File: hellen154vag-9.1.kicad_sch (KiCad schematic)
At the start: 219 parts, among them J1 USB_B_Mini, M1 Module-can-0.1, M2 Module-power5-0.1, M3 Module-mcu-0.1, M4 Module-input-0.1, M5 Module-knock-0.1, M6 Module-output-0.1, M7 Module-ign8-0.1, M8 Module-power12-0.1, P1 368255-2

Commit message: Updated to most recent VAG121 layout, which adds ETB and VR circuits.
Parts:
- removed V51, V52, V70, V71: Pad, hellen-one-common:PAD-TH, symbol hellen-one-common:Pad
- added BT1: BATTERY_CR2032, Battery:BatteryHolder_Keystone_1060_1x2032, symbol art-electro-power:BATTERY_CR2032
- added C1, C15, C16, C2, C6: 100n, hellen-one-common:C0603, symbol hellen-one-common:Cap
- added C10, C11, C12, C13, C14, C7, C8, C9: 10u, Capacitor_SMD:C_0805_2012Metric, symbol hellen-one-common:Cap
- added C17: 10u, hellen-one-common:C0603, symbol hellen-one-common:Cap
- added C3: 220n, hellen-one-common:C0603, symbol hellen-one-common:Cap
- added C4: 10n, hellen-one-common:C0603, symbol hellen-one-common:Cap
- added C5: 5.6n, hellen-one-common:C0603, symbol hellen-one-common:Cap
- added D1, D2, D3, D5, D9: 1N4148WS, hellen-one-common:SOD-323, symbol hellen-one-common:1N4148WS
- added D4, D6, D7, D8: LED-GREEN-0805, hellen-one-common:LED-0805, symbol hellen-one-common:LED
- added G1, G2, G3, G5: PROTO_AREA, hellen-one-common:PROTO_AREA, symbol hellen-one-common:PROTO_AREA
- added G6: LOGO, hellen-one-common:LOGO, symbol hellen-one-common:LOGO
- added J1: USB_B_Mini, hellen-one-common:USB-MINI-B-VERTICAL, symbol hellen-one-common:USB_B_Mini
- added J10: AudioJack_THR, hellen-one-common:Jack_3.5mm_PJ-3250-5A, symbol hellen-one-common:AudioJack_THR
- added J2, J3, J4, J5, J6: Conn_01x01, TestPoint:TestPoint_Pad_D2.0mm, symbol Connector_Generic:Conn_01x01
- added J7, J9: Conn_01x04, Connector_PinHeader_2.54mm:PinHeader_1x04_P2.54mm_Vertical, symbol Connector_Generic:Conn_01x04
- added J8: Conn_01x06, Connector_PinHeader_2.54mm:PinHeader_1x06_P2.54mm_Vertical, symbol Connector_Generic:Conn_01x06
- added M1, M10: Module-can-0.1, hellen-one-can-0.1:can, symbol hellen-one-can-0.1:Module-can-0.1
- added M11: Module-vr-0.1, hellen-one-vr-0.1:vr, symbol hellen-one-vr-0.1:Module-vr-0.1
- added M12: Module-dinput4-0.1, hellen-one-dinput4-0.1:dinput4, symbol hellen-one-dinput4-0.1:Module-dinput4-0.1
- added M2: Module-power5-0.2, hellen-one-power5-0.1:power5, symbol hellen-one-power5-0.1:Module-power5-0.1
- added M3: Module-mcu-0.1, hellen-one-mcu-0.1:mcu, symbol hellen-one-mcu-0.1:Module-mcu-0.1
- added M4: Module-input-0.1, hellen-one-input-0.1:input, symbol hellen-one-input-0.1:Module-input-0.1
- added M5: Module-knock-0.1, hellen-one-knock-0.1:knock, symbol hellen-one-knock-0.1:Module-knock-0.1
- added M6: Module-output-0.1, hellen-one-output-0.1:output, symbol hellen-one-output-0.1:Module-output-0.1
- added unit 3 of M6
- added M7: Module-ign8-0.1, hellen-one-ign8-0.1:ign8, symbol hellen-one-ign8-0.1:Module-ign8-0.1
- added M8: Module-power12-0.1, hellen-one-power12-0.1:power12, symbol hellen-one-power12-0.1:Module-power12-0.1
- added M9: Module-wbo-0.1, hellen-one-wbo-0.1:wbo, symbol hellen-one-wbo-0.1:Module-wbo-0.1
- added R1: 100, hellen-one-common:R0603, symbol hellen-one-common:Res
- added R10, R11, R12, R13: Jumper-Pad-Pad, hellen-one-common:PAD-0805-PAD, symbol hellen-one-common:Jumper-Pad-Pad
- added R14, R15: DNP, hellen-one-common:R1206, symbol hellen-one-common:Res
- added R16, R17: 5.1k, hellen-one-common:R0603, symbol hellen-one-common:Res
- added R18, R19: 4.7k, hellen-one-common:R0603, symbol hellen-one-common:Res
- added R20: 1.6k, hellen-one-common:R0603, symbol hellen-one-common:Res
- added R21: 750, hellen-one-common:R0603, symbol hellen-one-common:Res
- added R5: 100k, hellen-one-common:R0603, symbol hellen-one-common:Res
- added R6, R7: 2.7k, hellen-one-common:R0603, symbol hellen-one-common:Res
- added S1, S2: Button_SPST, hellen-one-common:SMD-2_2.9x3.9x1.7, symbol hellen-one-common:Button_SPST
- added U1: L6205PD, hellen-one-common:SO20POWER, symbol hellen-one-common:L6205PD
- added U2: LPS25HB, Package_LGA:ST_HLGA-10_2.5x2.5mm_P0.6mm_LayoutBorder3x2y, symbol Sensor_Pressure:LPS25HB
- added U3: MCP6002-xSN, Package_SO:SOIC-8_3.9x4.9mm_P1.27mm, symbol Amplifier_Operational:MCP6002-xSN
- added VIN1, VIN2, VIN3, VIN4, VOUT1, VOUT2, VOUT3: Pad, hellen-one-common:PAD-TH, symbol hellen-one-common:Pad
- P1: footprint rusEFI_Lib:284617-1 -> hellen121vag:368255-2
- R2, R3, R4, R8, R9: LCSC C17477 -> C17477
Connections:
- net +12V: now also D5.1 (K), D8.1 (A), G3.1, G3.11, G3.6, J2.1 (Pin_1), M2.V1 (V12), M8.V1 (V12)
- net +3V3: now also C15.2, D7.1 (A), G3.13, G3.3, G3.8, J4.1 (Pin_1), M3.N16 (V33), R18.1, R19.1, S1.2, U2.1 (VDDio), U2.10 (VDD), U2.6 (~CS)
- net +5V: now also C16.2, D6.1 (A), G3.12, G3.2, G3.7, J3.1 (Pin_1), M1.V1 (V5), M10.V1 (V5), M11.N1 (V5), M12.V1 (V5), M2.V2 (V5), M3.S1 (V5), M4.E2 (V5), M6.W14 (V5), M8.E1 (V5), M9.W1 (V5_IN), U3.8 (V+)
- net A1: now also M3.S30 (IN_O2S2), M4.N4 (O2S2)
- net A2: now also M3.S22 (IN_MAP3), M4.N12 (MAP3)
- net A3: now also M3.S26 (IN_AUX3), M4.N8 (AUX3)
- net A4: now also M3.S23 (IN_RES3), M4.N11 (RES3)
- net AFR: now also M3.S16 (IN_O2S), M4.N18 (O2S)
- net BOOT0: now also M3.N28 (BOOT0), S1.1
- net CAM1: now also M3.S15 (IN_CAM), M4.N19 (CAM)
- net CAM2: now also M3.S27 (IN_AUX4), M4.N7 (AUX4)
- net CAN_RX: now also M1.V6 (CAN_RX), M3.N2 (CAN_RX)
- net CAN_TX: now also M1.V5 (CAN_TX), M3.N3 (CAN_TX)
- net CAN_VIO: now also M1.V2 (CAN_VIO), M3.N1 (CAN_VIO)
- net CE: now also M3.E22 (OUT_IO8), M6.W25 (LOW6_DIODE)
- net CLT: now also M3.S18 (IN_CLT), M4.N16 (CLT)
- net CRANK: now also M3.S13 (IN_CRANK), M4.N21 (CRANK)
- net D1: now also M12.W4 (OUT_D1), M3.S3 (IN_D1)
- net D2: now also M12.W3 (OUT_D2), M3.S4 (IN_D2)
- net D3: now also M12.W2 (OUT_D3), M3.S5 (IN_D3)
- net D4: now also M12.W1 (OUT_D4), M3.S6 (IN_D4)
- net FUEL_CONSUM: now also M3.E19 (OUT_PWM7), M6.W22 (PP2)
- net GND: now also BT1.2 (-), C1.1, C10.1, C11.1, C12.1, C13.1, C14.1, C15.1, C16.1, C2.1, C5.1, C6.1, C7.1, C8.1, C9.1, G3.10, G3.14, G3.15, G3.4, G3.5, G3.9, J1.5 (GND), J10.S, J5.1 (Pin_1), J6.1 (Pin_1), J8.3 (Pin_3), M1.E1 (GND), M10.E1 (GND), M11.G (GND), M12.G (GND), M12.J1 (PULL_D1), M12.J2 (PULL_D2), M12.J3 (PULL_D3), M12.J4 (PULL_D4), M2.G (GND), M3.S2 (GND), M4.E1 (GND), M5.E2 (GND), M6.G (GND), M6.S3 (GND), M7.G (GND), M8.S1 (GND), M9.E6 (LSU_H-), M9.G (GND), R16.2, R17.2, R20.2, R21.2, S2.2, U1.1 (GND@1), U1.10 (GND@2), U1.11 (GND@3), U1.13 (SENSEB), U1.20 (GND@4), U1.8 (SENSEA), U1.SLUG1 (SLUG@1), U1.SLUG2 (SLUG@2), U1.SLUG3 (SLUG@3), U2.3 (GND), U2.5 (SA0/MISO), U2.8 (GND), U2.9 (GND), U3.4 (V-), U3.5 (+)
- net GNDA: now also M3.S32 (GNDA), M4.J11 (PULL_RES3), M4.J12 (PULL_MAP3), M4.J13 (PULL_MAP2), M4.J14 (PULL_MAP1), M4.J2 (PULL_GNDA), M4.J22 (PULL_KNOCK), M4.J24 (PULL_SENS3), M4.J3 (PULL_RES2), M4.J4 (PULL_O2S2), M4.J6 (PULL_RES1), M4.J8 (PULL_AUX3), M4.N2 (GNDA), R6.2, R7.2
- net IAT: now also M3.S19 (IN_IAT), M4.N15 (IAT)
- net IDLE: now also M3.E18 (OUT_PWM6), M6.W38 (LOW3_DUAL)
- net IGN1: now also M3.W1 (OUT_IGN1), M7.V8 (IGN1)
- net IGN2: now also M3.W2 (OUT_IGN2), M7.V7 (IGN2)
- net IGN3: now also M3.W3 (OUT_IGN3), M7.V6 (IGN3)
- net IGN4: now also M3.W4 (OUT_IGN4), M7.V5 (IGN4)
- net IGN5: now also M3.W5 (OUT_IGN5), M7.V4 (IGN5)
- net IGN6: now also M3.W6 (OUT_IGN6), M7.V3 (IGN6)
- net IGN7: now also M3.W7 (OUT_IGN7), M7.V2 (IGN7)
- net IGN8: now also M3.W8 (OUT_IGN8), M7.V1 (IGN8)
- net IGN_V33: now also M3.W10 (IGN_V33), M7.V10 (V33)
- net IGN_V5: now also M3.W9 (IGN_V5), M7.V9 (VCC)
- net INJ1: now also M3.E25 (OUT_INJ1)
- net INJ2: now also M3.E26 (OUT_INJ2)
- net INJ3: now also M3.E29 (OUT_INJ3)
- net INJ4: now also M3.E30 (OUT_INJ4)
- net INJ5: now also M3.E31 (OUT_INJ5)
- net INJ6: now also M3.E32 (OUT_INJ6)
- net INJ7: now also M3.E33 (OUT_INJ7)
- net INJ8: now also M3.E34 (OUT_INJ8)
- net IN_A1: now also M4.S25 (IN_O2S2), VIN1.1 (Pin_1)
- net IN_A2: now also M4.S19 (IN_MAP3), VIN2.1 (Pin_1)
- net IN_A3: now also M4.S20 (IN_AUX3), VIN3.1 (Pin_1)
- net IN_A4: now also M4.S22 (IN_RES3), VIN4.1 (Pin_1)
- net IN_AFR: now also M4.S9 (IN_O2S)
- net IN_CAM1: now also P1.86, M4.S5 (IN_CAM)
- net IN_CAM2: now also M4.S21 (IN_AUX4)
- net IN_CLT: now also P1.93, M4.S15 (IN_CLT), R6.1
- net IN_CRANK: now also M11.W2 (OUT_VR1), M4.S8 (IN_CRANK), R14.2; no longer P1.82
- net IN_D1: now also M12.V2 (IN_D1)
- net IN_D2: now also M12.V3 (IN_D2)
- net IN_D3: now also M12.V4 (IN_D3)
- net IN_D4: now also M12.V5 (IN_D4)
- net IN_IAT: now also P1.26, M4.S16 (IN_IAT), R7.1
- net IN_KNOCK1: now also M4.S7 (IN_KNOCK), M5.E3 (OUT_KNOCK), U3.3 (+)
- net IN_KNOCK1_RAW: now also M5.W1 (IN_KNOCK)
- net IN_KNOCK2: now also M4.S3 (IN_SENS3)
- net IN_MAF: now also P1.29, M4.S11 (IN_MAP1)
- net IN_MAP2: now also P1.101, M4.S12 (IN_MAP2)
- net IN_PPS1: now also M4.S24 (IN_PPS)
- net IN_PPS2: now also M4.S18 (IN_AUX2)
- net IN_RES1: now also M4.S23 (IN_RES1)
- net IN_RES2: now also M4.S26 (IN_RES2)
- net IN_TPS1: now also P1.92, M4.S10 (IN_TPS)
- net IN_TPS2: now also P1.84, M4.S17 (IN_AUX1)
- net IN_VIGN: now also D3.1 (K), D4.1 (A), M8.V3 (IN_VIGN)
- net IN_VSS: now also M4.S6 (IN_VSS)
- net KNOCK1: now also M3.S12 (IN_KNOCK), M4.N22 (KNOCK)
- net KNOCK2: now also M4.N24 (SENS3)
- net MAF: now also M3.S20 (IN_MAP1), M4.N14 (MAP1)
- net MAIN: now also M3.E6 (OUT_IO3), M6.W40 (LOW5_MAIN)
- net MAP2: now also M3.S21 (IN_MAP2), M4.N13 (MAP2)
- net NRESET: now also C6.2, M3.N24 (nReset), S2.1
- net OUT1: now also M3.E7 (OUT_IO5), M6.W39 (LOW7_HIGH1)
- net OUT2: now also M3.E9 (OUT_IO6), M6.W37 (LOW8_HIGH2)
- net OUT3: now also M3.E28 (OUT_PWM8), M6.W21 (LOW1)
- net OUT_COIL_A1: no longer P1.117
- net OUT_COIL_A2: no longer P1.118
- net OUT_FUEL_CONSUM: now also M6.S6 (OUT_PP2)
- net OUT_IGN1: now also P1.102, M7.S8 (OUT_IGN1)
- net OUT_IGN2: now also P1.7, M7.S7 (OUT_IGN2)
- net OUT_IGN3: now also P1.111, M7.S6 (OUT_IGN3)
- net OUT_IGN4: now also P1.94, M7.S5 (OUT_IGN4)
- net OUT_IGN5: now also M7.S4 (OUT_IGN5)
- net OUT_IGN6: now also M7.S3 (OUT_IGN6)
- net OUT_IGN7: now also M7.S2 (OUT_IGN7)
- net OUT_IGN8: now also M7.S1 (OUT_IGN8)
- net OUT_PUMP: now also M6.S10 (OUT_LOW11)
- net OUT_TACH: now also M6.W6 (OUT_PP1)
- net OUT_VVT1_1: now also M6.S13 (OUT_LOW12), M6.S14 (OUT_LOW9)
- net OUT_VVT1_2: now also M6.W1 (OUT_LOW2), M6.W2 (OUT_LOW10)
- net OUT_VVT2_B1: now also M6.S5 (OUT_SOLENOID_B2)
- net OUT_VVT2_B2: now also M6.S4 (OUT_SOLENOID_B1)
- net OUT_WASTEGATE: now also P1.104
- net PPS1: now also M3.S29 (IN_PPS), M4.N5 (PPS)
- net PPS2: now also M3.S25 (IN_AUX2), M4.N9 (AUX2)
- net PUMP: now also M3.E8 (OUT_IO1), M6.W35 (LOW11)
- net RES1: now also M3.S28 (IN_RES1), M4.N6 (RES1)
- net RES2: now also M3.S31 (IN_RES2), M4.N3 (RES2)
- net TACH: now also M3.E27 (OUT_PWM1), M6.W28 (PP1)
- net TPS1: now also M3.S17 (IN_TPS), M4.N17 (TPS)
- net TPS2: now also M3.S24 (IN_AUX1), M4.N10 (AUX1)
- net USBM: now also J1.2 (D-), M3.N31 (USB1M)
- net USBP: now also J1.3 (D+), M3.N30 (USB1P)
- net V12_PERM: now also M8.V4 (V12_PERM)
- net V12_RAW: no longer F1.2, F2.2
- net V5A: no longer P1.53, P1.73, P1.83, P1.98
- net VBAT: now also D9.1 (K), M3.N17 (VBAT), M8.V2 (VBAT)
- net VBUS: now also J1.1 (VBUS), M3.N29 (VBUS)
- net VIGN: now also M3.S7 (VIGN), M8.V5 (VIGN)
- net VREF1: now also M4.S14 (VREF1), R15.2
- net VREF2: now also M4.S13 (VREF2), M5.W2 (VREF)
- net VSS: now also M3.S14 (IN_VSS), M4.N20 (VSS)
- net VVT1_1: now also M3.E10 (OUT_IO10), M6.W27 (LOW9), M6.W36 (LOW12)
- net VVT1_2: now also M3.E21 (OUT_IO7), M6.W26 (LOW10), M6.W29 (LOW2)
- net VVT2_B1: now also M3.E17 (OUT_PWM5), M6.W30 (SOLENOID_B2)
- net VVT2_B2: now also M3.E16 (OUT_PWM4), M6.W31 (SOLENOID_B1)
- net WASTEGATE: now also M3.E12 (OUT_IO2), M6.W34 (LOW4_DUAL)
- net at P1.21: now also R2.1, R8.1
- net at P1.23: now also R3.1
- net at P1.51: now also R10.1
- net at P1.52: now also R11.1
- net CAN-: now reaches P1.58
- net CAN-: now also M1.S1 (CANL), M10.S1 (CANL)
- net CAN+: now reaches P1.60
- net CAN+: now also M1.S2 (CANH), M10.S2 (CANH)
- net at P1.70: now also R12.1
- net at P1.71: now also R13.1
- net +5VA: now reaches P1.72
- net +5VA: now also P1.53, P1.73, P1.83, P1.98, M3.S33 (V5A), M4.E5 (V5A), M4.J1 (PULL_V5A), M4.J10 (PULL_AUX1), M4.J17 (PULL_CAM), M4.J18 (PULL_VSS), M4.J19 (PULL_TPS), M4.J20 (PULL_O2S), M4.J21 (PULL_CRANK), M4.J5 (PULL_PPS), M4.J7 (PULL_AUX4), M4.J9 (PULL_AUX2), M4.N1 (V5A), M5.E1 (V5A)
- net IN_CRANK-: now reaches P1.90
- net IN_CRANK-: now also M11.E1 (IN_VR1-), R15.1
- net LSU_HEAT-: now reaches P1.5
- net LSU_HEAT-: now also M9.E5 (LSU_H+)
- new net: BT1.1 (+), D9.2 (A)
- new net: D5.2 (A), D8.2 (K), R17.1
- new net: D6.2 (K), R20.1
- new net: G5.1, G5.11, G5.6
- new net: G5.10, G5.15, G5.5
- new net: G5.12, G5.2, G5.7
- new net: G5.13, G5.3, G5.8
- new net: G5.14, G5.4, G5.9
- new net: D3.2 (A), D4.2 (K), R16.1
- new net: G1.1, G1.11, G1.6
- new net: G1.10, G1.15, G1.5
- new net: G1.12, G1.2, G1.7
- new net: G1.13, G1.3, G1.8
- new net: G1.14, G1.4, G1.9
- new net: M3.N18 (I2C_SDA), R19.2, U2.4 (SDA/MOSI)
- new net: M3.N19 (I2C_SCL), R18.2, U2.2 (SCL/SCLK)
- new net: U3.6 (-), U3.7
- new net: C5.2, R5.2, U1.16 (ENB), U1.5 (ENA)
- new net: M6.S8 (OUT_LOW1), VOUT3.1 (Pin_1)
- new net: M6.S12 (OUT_LOW8_PULLUP), VOUT2.1 (Pin_1)
- new net: D1.1 (K), D2.2 (A), R1.1
- new net: C4.1, U1.4 (VCP)
- new net: C4.2, R1.2
- new net: M6.W9 (OUT_LOW7_PULLUP), VOUT1.1 (Pin_1)
- new net: C17.2, U3.1, U3.2 (-)
- new net: C17.1, J10.T
- new net: C3.1, D2.1 (K), U1.17 (VBOOT)
- new net: G2.1, G2.11, G2.6
- new net: G2.10, G2.15, G2.5
- new net: G2.12, G2.2, G2.7
- new net: G2.13, G2.3, G2.8
- new net: G2.14, G2.4, G2.9
- new net: D7.2 (K), R21.1
- new net: M10.V2 (CAN_VIO), M9.W2 (CAN_VIO)
- new net: M10.V6 (CAN_RX), M9.W3 (CAN_RX)
- new net: M10.V5 (CAN_TX), M9.W4 (CAN_TX)
- new net: J8.5 (Pin_5), M9.W5 (nReset)
- new net: J8.4 (Pin_4), M9.W6 (SWDIO)
- new net: J8.2 (Pin_2), M9.W7 (SWCLK)
- new net: J8.1 (Pin_1), M9.W8 (V33_OUT)
- new net +12V_PROT: M6.W5 (V12P)
- new net +12V_RAW: C1.2, C10.2, C11.2, C12.2, C13.2, C14.2, C2.2, C3.2, C7.2, C8.2, C9.2, D1.2 (A), F1.2, F2.2, M6.S11 (V12_RAW), M8.E2 (V12_RAW), U1.19 (VSB), U1.2 (VSA)
- new net +ETB: M3.E14 (OUT_PWM2), U1.15 (IN2B), U1.7 (IN2A)
- new net +ETB_OUT: P1.117, U1.18 (OUT2B), U1.3 (OUT2A)
- new net -ETB: M3.E15 (OUT_PWM3), U1.14 (IN1B), U1.6 (IN1A)
- new net -ETB_OUT: P1.118, U1.12 (OUT1B), U1.9 (OUT1A)
- new net ETB_EN: M3.E13 (OUT_IO12), R5.1
- new net IN_CRANK+: M11.E2 (IN_VR1+), P1.82, R14.1
- new net IO1: J9.4 (Pin_4), M3.N12 (IO1)
- new net IO2: J9.3 (Pin_3), M3.N13 (IO2)
- new net IO3: J9.2 (Pin_2), M3.N14 (IO3)
- new net IO4: J9.1 (Pin_1), M3.N15 (IO4)
- new net LSU_CALIBR_RES: M9.E4 (LSU_Rtrim), R13.2
- new net LSU_PUMP_I: M9.E3 (LSU_Ip), R11.2
- new net LSU_SENSOR_U: M9.E1 (LSU_Un), R12.2
- new net LSU_SENSOR_U/PUMP_I: M9.E2 (LSU_Vm), R10.2
- new net SPI2_CS: J7.1 (Pin_1), M3.N23 (SPI2_CS)
- new net SPI2_MISO: J7.3 (Pin_3), M3.N21 (SPI2_MISO)
- new net SPI2_MOSI: J7.2 (Pin_2), M3.N22 (SPI2_MOSI)
- new net SPI2_SCK: J7.4 (Pin_4), M3.N20 (SPI2_SCK)
- no-connect marks 72 -> 126
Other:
- note added: "Analog inputs (sensors)"
- note added: "Board info"
- note added: "Bus types"
- note added: "Discrete inputs"
- note added: "ETB driver"
- note added: "General purpose bus"
- note added: "Ignition"
- note added: "Injection"
- note added: "LEDs"
- note added: "Ouputs"
- note added: "Power"
- note added: "Prototype areas"
- note added: "http://rusefi.com/s/hellen121vag"
- note added: "to ETB driver"
- moved on the sheet: C1, D1, J1, M1, M2, M3A, M3B, M3C, M3D, M4A, M4B, M4C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

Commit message: MISC net names were connected, like ETB and VR nets are now connected.
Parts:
- removed C1: Cap, hellen-one-common:C0603, symbol hellen-one-common:Cap
- removed D1: D_TVS_Array_4, hellen-one-common:SOT23-6, symbol hellen-one-common:D_TVS_Array_4
- removed J1: USB_B_Mini, hellen-one-common:USB-MINI-B-VERTICAL, symbol hellen-one-common:USB_B_Mini
- removed M1: Module-can-0.1, hellen-one-can-0.1:can, symbol hellen-one-can-0.1:Module-can-0.1
- removed M2: Module-power5-0.1, hellen-one-power5-0.1:power5, symbol hellen-one-power5-0.1:Module-power5-0.1
- removed M3: Module-mcu-0.1, hellen-one-mcu-0.1:mcu, symbol hellen-one-mcu-0.1:Module-mcu-0.1
- removed M4: Module-input-0.1, hellen-one-input-0.1:input, symbol hellen-one-input-0.1:Module-input-0.1
- removed M5: Module-knock-0.1, hellen-one-knock-0.1:knock, symbol hellen-one-knock-0.1:Module-knock-0.1
- removed M6: Module-output-0.1, hellen-one-output-0.1:output, symbol hellen-one-output-0.1:Module-output-0.1
- removed M7: Module-ign8-0.1, hellen-one-ign8-0.1:ign8, symbol hellen-one-ign8-0.1:Module-ign8-0.1
- removed M8: Module-power12-0.1, hellen-one-power12-0.1:power12, symbol hellen-one-power12-0.1:Module-power12-0.1
- removed R1, R5: Res_Array_4, hellen-one-common:R0603-4, symbol hellen-one-common:Res_Array_4
- removed R6, R7: Res, hellen-one-common:R0603, symbol hellen-one-common:Res
- removed S1, S2: Button_SPST, hellen-one-common:SMD-2_2.9x3.9x1.7, symbol hellen-one-common:Button_SPST
- removed VIN1, VIN2, VIN3, VIN4, VOUT1, VOUT2, VOUT3: Pad, hellen-one-common:PAD-TH, symbol hellen-one-common:Pad
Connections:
- net +ETB_OUT: now also W?.2
- net -ETB_OUT: now also W?.2
- net CAN+: no longer M1.S2 (CANH)
- net CAN-: no longer M1.S1 (CANL)
- net CANH: now also M1.S2 (CANH)
- net CANL: now also M1.S1 (CANL)
- net INJ6: now also M6.W17 (INJ6)
- net INJ7: now also M6.W16 (INJ7)
- net INJ8: now also M6.W15 (INJ8)
- net OUT_CE: now also M6.W3 (OUT_LOW6_DIODE)
- net OUT_IDLE: now also M6.S7 (OUT_LOW3_DUAL)
- net OUT_INJ6: now also M6.S15 (OUT_INJ6)
- net OUT_INJ7: now also M6.W12 (OUT_INJ7), W?.2
- net OUT_INJ8: now also M6.W11 (OUT_INJ8), W?.2
- net OUT_MAIN: now also M6.W13 (OUT_LOW5_MAIN)
- net OUT_WASTEGATE: now also M6.W4 (OUT_LOW4_DUAL)
- no-connect marks 126 -> 72

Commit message: This time I really did connect the VR net.
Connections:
- net IN_CRANK+: now also W?.2
- net IN_CRANK-: now also W?.2
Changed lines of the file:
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@@
     (stroke (width 0) (type solid) (color 0 0 0 0))
   )
+  (wire (pts (xy 45.72 278.13) (xy 56.515 278.13))
+    (stroke (width 0) (type solid) (color 0 0 0 0))
+  )
   (wire (pts (xy 45.72 344.17) (xy 51.435 344.17))
     (stroke (width 0) (type solid) (color 0 0 0 0))
@@
     (effects (font (size 1.27 1.27)) (justify left bottom))
   )
+  (label "IN_CRANK+" (at 45.72 280.67 0)
+    (effects (font (size 1.27 1.27)) (justify left bottom))
+  )
   (label "INJ_B2_HIGH" (at 45.72 289.56 0)
     (effects (font (size 1.27 1.27)) (justify left bottom))
@@
     (effects (font (size 1.27 1.27)) (justify left bottom))
   )
+  (label "IN_CRANK-" (at 45.72 322.58 0)
+    (effects (font (size 1.27 1.27)) (justify left bottom))
+  )
   (label "INJ_B1_HIGH" (at 45.72 331.47 0)
     (effects (font (size 1.27 1.27)) (justify left bottom))
@@
       (effects (font (size 1.27 1.27)) hide)
     )
-    (property "Value" "V5A" (id 1) (at 50.0444 320.4083 0))
+    (property "Value" "V5A" (id 1) (at 50.0444 319.7733 90))
     (property "Footprint" "" (id 2) (at 45.72 320.04 0)
       (effects (font (size 1.27 1.27)) hide)
@@
     (pin "1")
   )
-  (symbol (lib_id "power:GND") (at 45.72 278.13 90) (unit 1)
-    (in_bom yes) (on_board yes)
-    (property "Reference" "#PWR?" (id 0) (at 52.07 278.13 0)
-      (effects (font (size 1.27 1.27)) hide)
-    )
-    (property "Value" "GND" (id 1) (at 49.6634 278.0792 0))
-    (property "Footprint" "" (id 2) (at 45.72 278.13 0)
-      (effects (font (size 1.27 1.27)) hide)
-    )
-    (property "Datasheet" "" (id 3) (at 45.72 278.13 0)
-      (effects (font (size 1.27 1.27)) hide)
-    )
-    (pin "1")
-  )
   (symbol (lib_id "power:GND") (at 50.8 386.08 90) (unit 1)
     (in_bom yes) (on_board yes)
@@
     (pin "1")
   )
+  (symbol (lib_id "power:GND") (at 56.515 278.13 90) (unit 1)
+    (in_bom yes) (on_board yes)
+    (property "Reference" "#PWR?" (id 0) (at 62.865 278.13 0)
+      (effects (font (size 1.27 1.27)) hide)
+    )
+    (property "Value" "GND" (id 1) (at 60.4584 278.0792 0))
+    (property "Footprint" "" (id 2) (at 56.515 278.13 0)
+      (effects (font (size 1.27 1.27)) hide)
+    )
+    (property "Datasheet" "" (id 3) (at 56.515 278.13 0)
+      (effects (font (size 1.27 1.27)) hide)
+    )
+    (pin "1")
+  )
   (symbol (lib_id "power:GNDA") (at -417.195 80.645 90) (mirror x) (unit 1)
     (in_bom yes) (on_board yes)
@@
   )
   (symbol (lib_id "hellen-one-dinput4-0.1:Module-dinput4-0.1") (at 198.12 300.355 0) (unit 1)
-    (in_bom yes) (on_board yes) (fields_autoplaced)
-    (property "Reference" "M12" (id 0) (at 214.63 297.0488 0))
-    (property "Value" "Module-dinput4-0.1" (id 1) (at 214.63 299.3475 0))
+    (in_bom yes) (on_board yes)
+    (property "Reference" "M12" (id 0) (at 213.995 310.3838 0))
+    (property "Value" "Module-dinput4-0.1" (id 1) (at 214.63 312.6825 0))
     (property "Footprint" "hellen-one-dinput4-0.1:dinput4" (id 2) (at 198.12 300.355 0)
       (effects (font (size 1.27 1.27)) hide)
@@
   )
   (symbol (lib_name "hellen-one-input-0.1:Module-input-0.1_4") (lib_id "hellen-one-input-0.1:Module-input-0.1") (at 198.12 216.535 0) (unit 3)
-    (in_bom yes) (on_board yes) (fields_autoplaced)
-    (property "Reference" "M4" (id 0) (at 213.9951 256.4141 0)
+    (in_bom yes) (on_board yes)
+    (property "Reference" "M4" (id 0) (at 207.6451 255.1441 0)
       (effects (font (size 1.27 1.27)) (justify left))
     )
-    (property "Value" "Module-input-0.1" (id 1) (at 213.9951 258.7128 0)
+    (property "Value" "Module-input-0.1" (id 1) (at 205.1051 256.8078 0)
       (effects (font (size 1.27 1.27)) (justify left))
     )

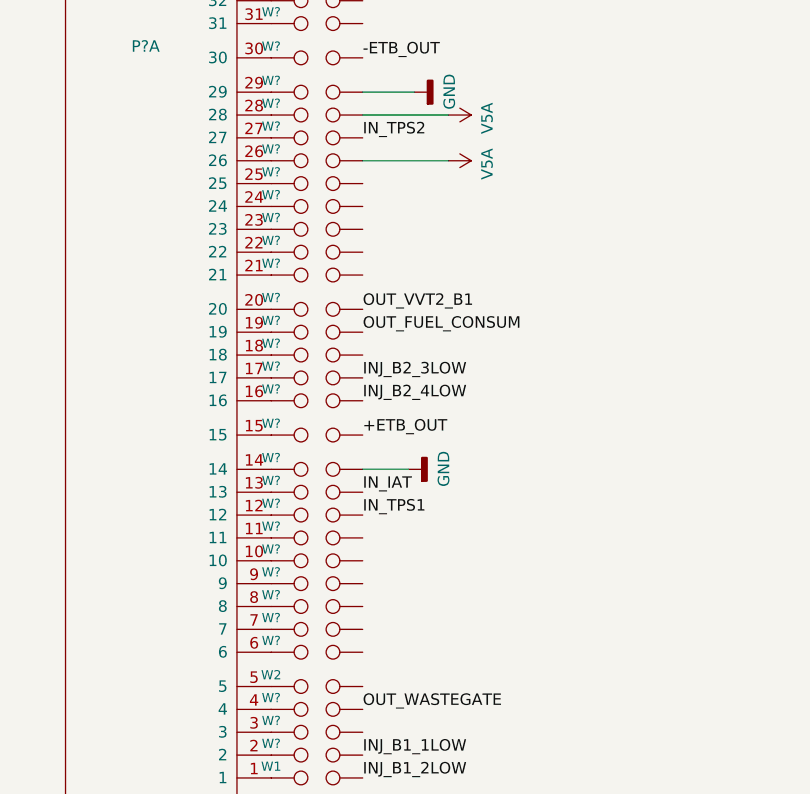
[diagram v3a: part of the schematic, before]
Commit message: Connected IN_RES1 and IN_RES2 as fuel pump analog inputs.
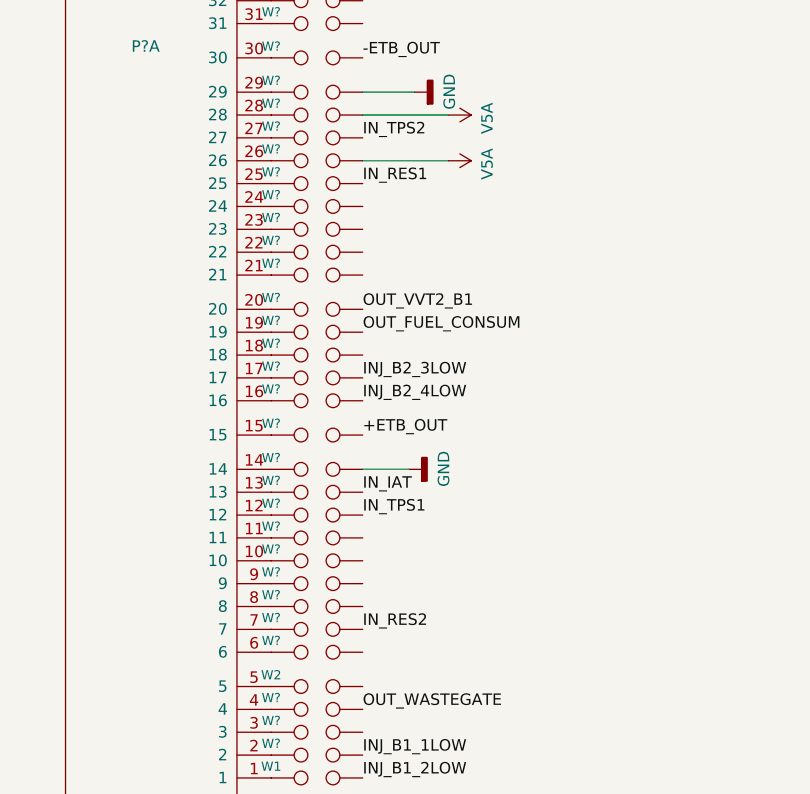
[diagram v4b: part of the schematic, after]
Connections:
- net IN_RES1: now also W?.2
- net IN_RES2: now also W?.2
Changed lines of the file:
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@@
+    (effects (font (size 1.27 1.27)) (justify left bottom))
+  )
+  (label "IN_RES1" (at 45.72 354.33 0)
     (effects (font (size 1.27 1.27)) (justify left bottom))
   )
@@
     (effects (font (size 1.27 1.27)) (justify left bottom))
   )
+  (label "IN_RES2" (at 45.72 403.86 0)
+    (effects (font (size 1.27 1.27)) (justify left bottom))
+  )

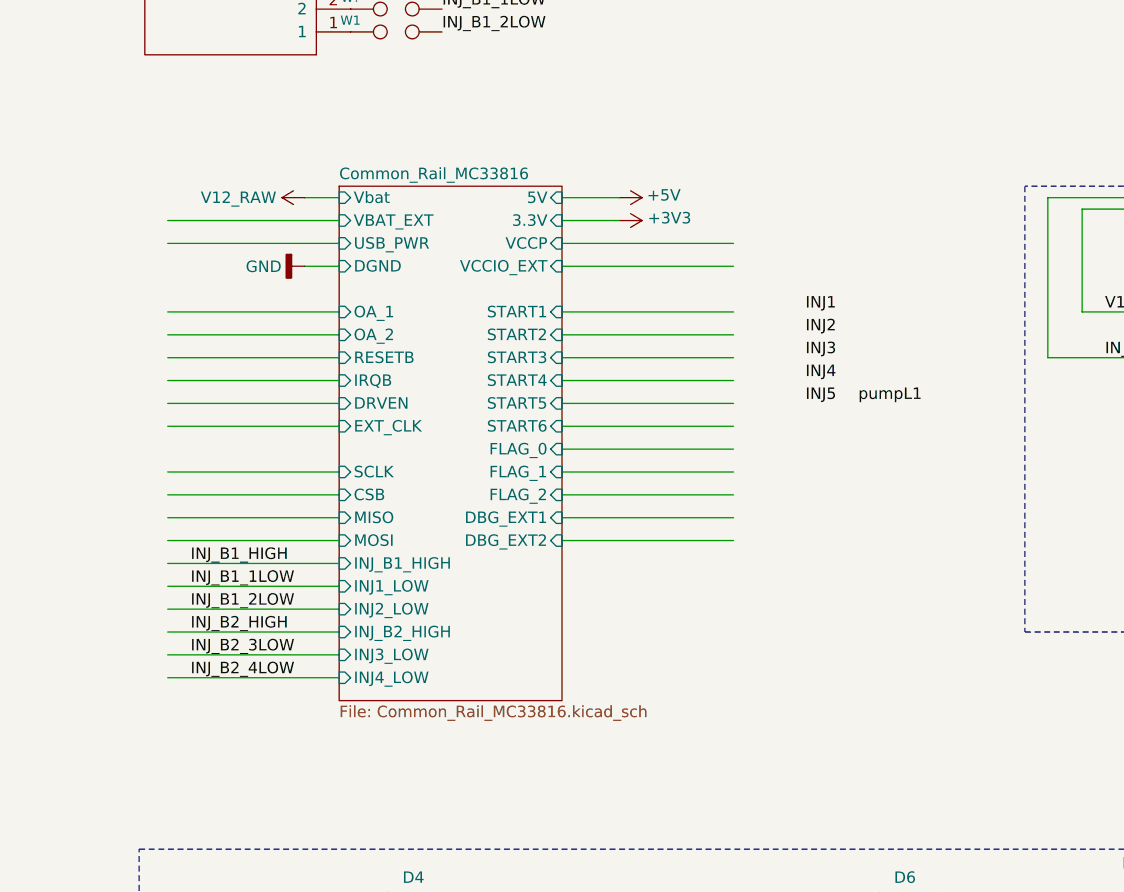
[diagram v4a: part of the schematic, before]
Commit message: DI IO are mostly connected, nets with titles like this need to be connected to STM32 TBD_### https://github.com/rusefi/hellen154vag-9.1/issues/4
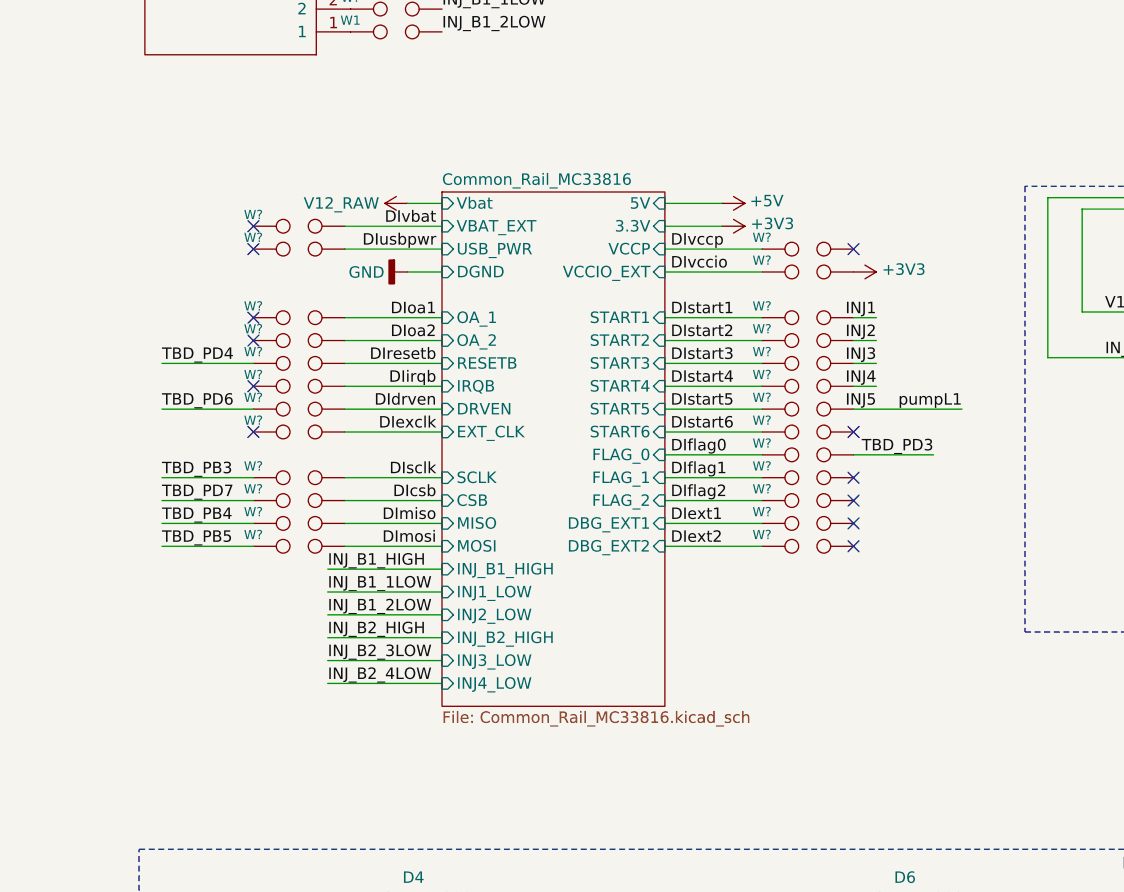
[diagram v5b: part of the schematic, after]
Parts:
- added W? (x25): TEST, rusEFI_Lib:SM0805_jumper, symbol hellen-one-common:TEST
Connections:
- net +3V3: now also W?.2
- net INJ1: now also W?.2
- net INJ2: now also W?.2
- net INJ3: now also W?.2
- net INJ4: now also W?.2
- net INJ5: now also W?.2
- new net DIcsb: W?.2
- new net DIdrven: W?.2
- new net DIexclk: W?.2
- new net DIext1: W?.1
- new net DIext2: W?.1
- new net DIflag0: W?.1
- new net DIflag1: W?.1
- new net DIflag2: W?.1
- new net DIirqb: W?.2
- new net DImiso: W?.2
- new net DImosi: W?.2
- new net DIoa1: W?.2
- new net DIoa2: W?.2
- new net DIresetb: W?.2
- new net DIsclk: W?.2
- new net DIstart1: W?.1
- new net DIstart2: W?.1
- new net DIstart3: W?.1
- new net DIstart4: W?.1
- new net DIstart5: W?.1
- new net DIstart6: W?.1
- new net DIusbpwr: W?.2
- new net DIvbat: W?.2
- new net DIvccio: W?.1
- new net DIvccp: W?.1
- new net TBD_PB3: W?.1
- new net TBD_PB4: W?.1
- new net TBD_PB5: W?.1
- new net TBD_PD3: W?.2
- new net TBD_PD4: W?.1
- new net TBD_PD6: W?.1
- new net TBD_PD7: W?.1
- no-connect marks 72 -> 84
